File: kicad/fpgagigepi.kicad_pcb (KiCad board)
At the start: 4 copper layers, 65 x 56 mm, 142 parts, among them J1 BH-10(IDC-10MS), J2 PLS-2, J3 PBD-40(DS1023-2x20), J4 PLD-10(DS1021-2x5), J5 L829-1J1T-43, J6 POE connector, J7 PLS-1, J8 PLS-1, J9 PLS-1, U1 CAT24C32WI, U10 TLV62084DSGR, U11 TLV62084DSGR, U2 ASEMB-25.000MHZ-LC-T, U3 NUP4114UPXV6T1G, U4 NB3L553MNR, U5 10CL025ZE144, U6 KSZ9021GN, U7 NUP4114UPXV6T1G, U8 NUP4114UPXV6T1G, U9 TLV62084DSGR

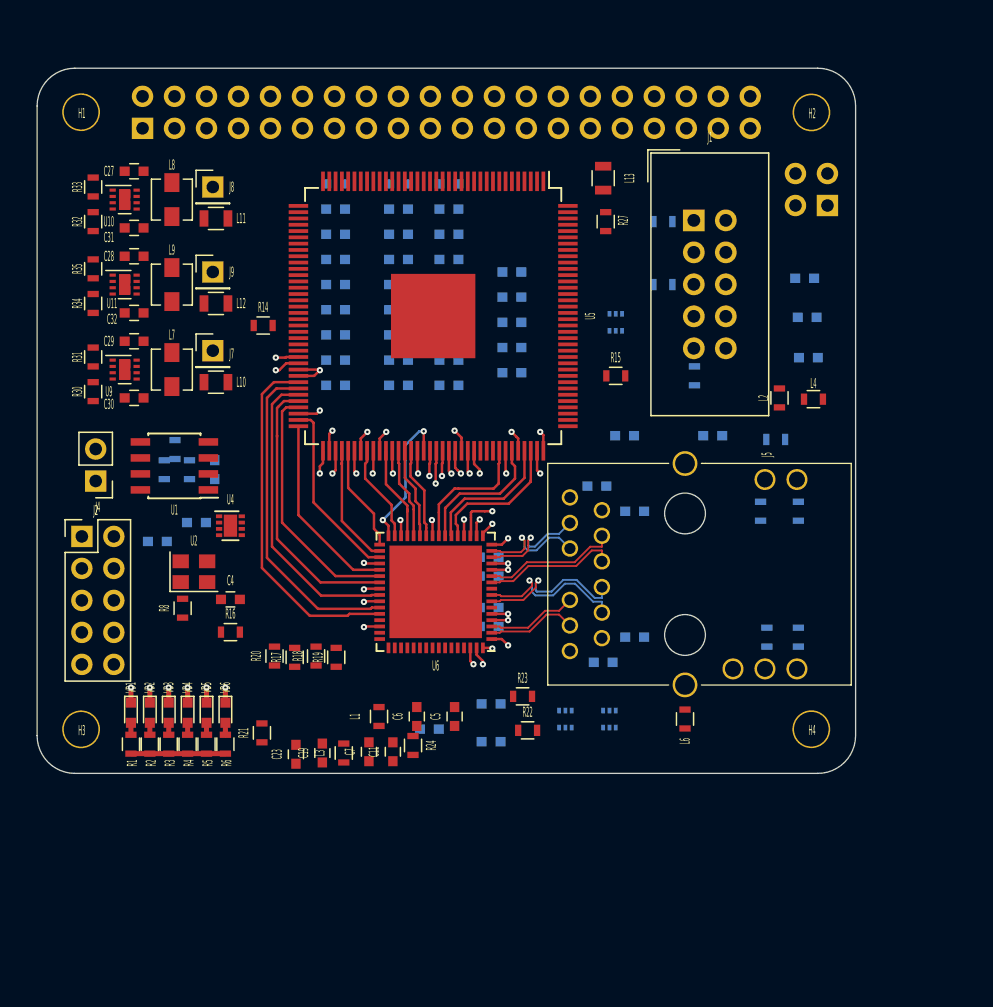
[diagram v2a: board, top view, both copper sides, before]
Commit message: Replaced clock buffer NB3L553DR2G to cdclvc1102 Added datasheet for cdclvc1102 Added components cdclvc1102pw in library_cache Remaped cyclone-to-40-pin-header connections Updated schematics Updated PCB - all signal routed. Power connections not routed Updated BOM file (non-altium format)
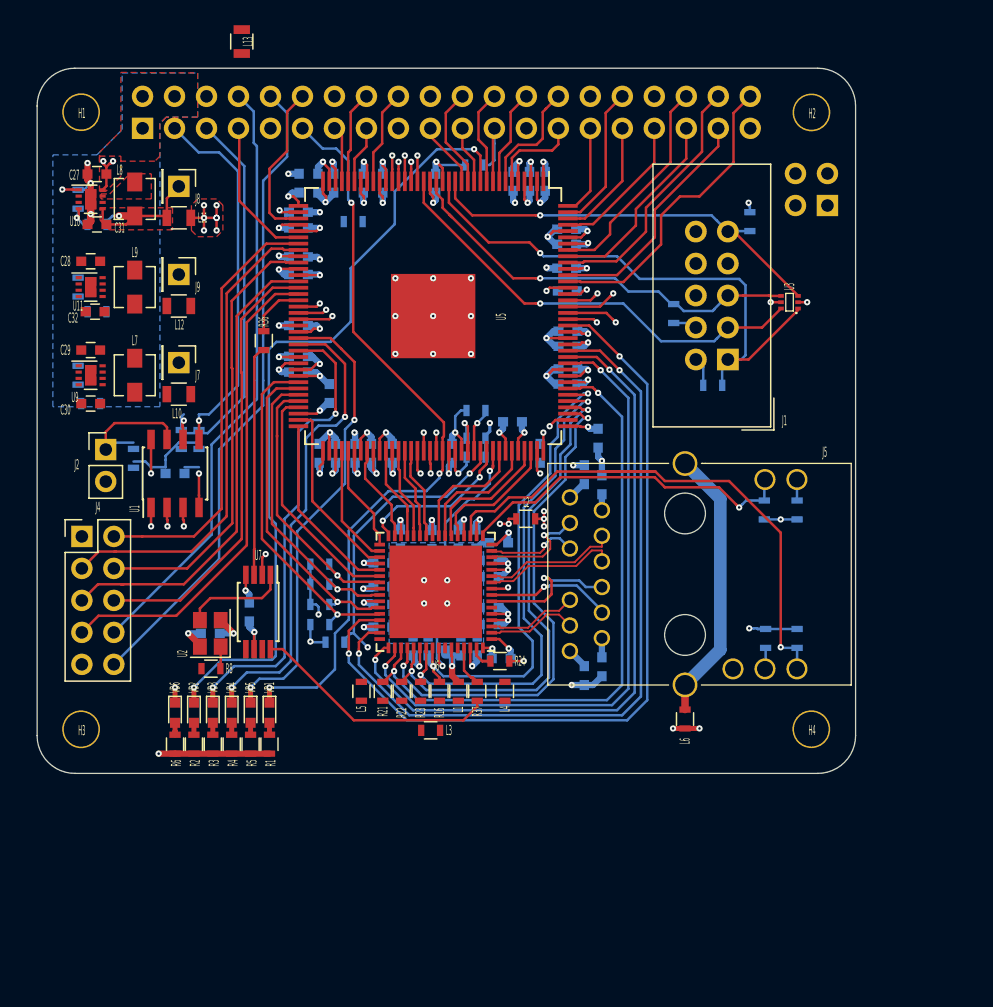
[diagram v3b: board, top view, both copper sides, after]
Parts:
- removed U4: NB3L553MNR, Housings_DFN_QFN:DFN-8-1EP_2x2mm_Pitch0.5mm
- removed U8: NUP4114UPXV6T1G, library:SOT-563-6
- added C65: 0.1u, Capacitors_SMD:C_0603, B.Cu at (103.8, 91.4)
- added C66: 0.1u, Capacitors_SMD:C_0603, B.Cu at (101.8, 86.7)
- added R36: 33R, Resistors_SMD:R_0603, F.Cu at (96.5, 82.5)
- added R37: 33R, Resistors_SMD:R_0603, F.Cu at (113.5, 110.3)
- added R38: 33R, Resistors_SMD:R_0603, B.Cu at (113.4, 91.7)
- added R39: 33R, Resistors_SMD:R_0603, B.Cu at (113.4, 90.2)
- added R40: 33R, Resistors_SMD:R_0603, B.Cu at (113.4, 88.0)
- C11, C19, C23, C4, C5, C6, C7, R14, R15, R17, R18, R19, R20, R27, R30, R31, R32, R33, R34, R35: moved to B.Cu
- L5, U3: moved to F.Cu
- U7: value NUP4114UPXV6T1G -> CDCLVC1102PW; footprint library:SOT-563-6 -> Housings_SSOP:TSSOP-8_4.4x3mm_Pitch0.65mm; moved to F.Cu
- moved R27 39.7 mm to (102.2, 106.4), turned to 0 degrees
- moved L5 38.5 mm to (104.3, 110.3), turned to 270 degrees
- moved C22 37.0 mm to (113.5, 106.7), turned to 90 degrees
- moved C18 34.2 mm to (115.4, 107.7), turned to 180 degrees
- moved L4 33.7 mm to (115.7, 110.3), turned to 270 degrees
- moved C10 32.1 mm to (115.2, 98.5), turned to 180 degrees
- moved L13 30.7 mm to (94.8, 58.7), turned to 90 degrees
- moved U7 25.8 mm to (96.1, 104.0), turned to 270 degrees
- moved L2 22.3 mm to (117.3, 96.6), turned to 0 degrees
- moved C23 22.3 mm to (113.4, 98.2), turned to 270 degrees
- moved C63 21.9 mm to (106.8, 91.4), turned to 90 degrees
- moved C9 21.8 mm to (112.0, 98.2), turned to 270 degrees
- moved C57 20.7 mm to (102.1, 70.0), turned to 270 degrees
- moved R15 20.1 mm to (113.3, 68.5), turned to 180 degrees
- moved C37 20.0 mm to (123.1, 90.2), turned to 270 degrees
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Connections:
- net AVDDL renamed /ethernet.sch/AVDDL
- net DVDDL renamed /ethernet.sch/DVDDL
- net Net-(C10-Pad1) renamed /ethernet.sch/AVDDH
- net Net-(C30-Pad1) renamed /power.sch/2.5V_out
- net Net-(C31-Pad1) renamed /power.sch/3.3V_out
- net Net-(C32-Pad1) renamed /power.sch/1.2V_out
- net Net-(C5-Pad1) renamed /ethernet.sch/AVDDL_PLL
- C3 pad 1: +3V3 -> GND
- C3 pad 2: GND -> +3V3
- J3 pad 12: IO_51 -> IO_39
- J3 pad 13: nSTATUS -> IO_99
- J3 pad 15: nCONFIG -> IO_85
- J3 pad 16: IO_6 -> IO_86
- J3 pad 18: IO_8 -> IO_87
- J3 pad 19: DATA -> nCONFIG
- J3 pad 21: IO_99 -> DCLK
- J3 pad 22: IO_85 -> DATA
- J3 pad 23: DCLK -> nSTATUS
- J3 pad 24: IO_86 -> IO_10
- J3 pad 25: Net-(J3-Pad25) -> GND
- J3 pad 26: IO_87 -> IO_8
- J3 pad 27: Net-(J3-Pad27) -> IO_6
- J3 pad 28: Net-(J3-Pad28) -> IO_7
- J3 pad 29: IO_76 -> IO_144
- J3 pad 31: IO_77 -> IO_142
- J3 pad 32: IO_98 -> IO_143
- J3 pad 33: IO_80 -> IO_141
- J3 pad 37: IO_83 -> IO_133
- J3 pad 39: Net-(J3-Pad25) -> GND
- J3 pad 7: IO_50 -> IO_42
- J3 pad 9: Net-(J3-Pad25) -> GND
- J4 pad 1: +5V -> +3V3
- J4 pad 2: /interface.sch/IO_44 -> /interface.sch/IO_43
- J4 pad 3: /interface.sch/IO_39 -> /interface.sch/IO_44
- J4 pad 5: /interface.sch/IO_42 -> /interface.sch/IO_49
- J4 pad 6: /interface.sch/IO_49 -> /interface.sch/IO_50
- J4 pad 7: /interface.sch/IO_43 -> /interface.sch/IO_51
- R27 pad 2: /ethernet.sch/RX_CLK -> RX_CLK
- U3 pad 1: JTAG_TDO -> JTAG_TCK
- U3 pad 3: JTAG_TMS -> JTAG_TDI
- U3 pad 4: JTAG_TDI -> JTAG_TMS
- U3 pad 6: JTAG_TCK -> JTAG_TDO
- U5 pad 10: USER_LED0 -> IO_10
- U5 pad 100: Net-(U5-Pad100) -> TX_CLK
- U5 pad 11: USER_LED1 -> USER_LED0
- U5 pad 111: Net-(U5-Pad111) -> /ethernet.sch/COL
- U5 pad 112: IO_76 -> INT_N
- U5 pad 113: IO_77 -> CLK_125M
- U5 pad 114: IO_80 -> /ethernet.sch/RESET_N
- U5 pad 115: IO_83 -> /ethernet.sch/MDIO
- U5 pad 119: IO_85 -> /ethernet.sch/MDC
- U5 pad 120: IO_86 -> /ethernet.sch/CRS
- U5 pad 121: IO_87 -> /ethernet.sch/RX_ER
- U5 pad 125: Net-(U5-Pad125) -> /ethernet.sch/RX_DV
- U5 pad 132: Net-(U5-Pad132) -> PI_GPIO21/SPI1_SCLK
- U5 pad 133: Net-(U5-Pad133) -> IO_133
- U5 pad 135: /ethernet.sch/RX_DV -> PI_GPIO20/SPI1_MOSI
- U5 pad 136: /ethernet.sch/RX_ER -> PI_GPIO19/SPI1_MISO
- U5 pad 137: /ethernet.sch/COL -> PI_GPIO16/SPI1_CS0
- U5 pad 141: /ethernet.sch/CRS -> IO_141
- U5 pad 142: /ethernet.sch/MDC -> IO_142
- U5 pad 143: /ethernet.sch/MDIO -> IO_143
- U5 pad 144: /ethernet.sch/RESET_N -> IO_144
- U5 pad 28: PI_GPIO19/SPI1_MISO -> IO_87
- U5 pad 31: PI_GPIO20/SPI1_MOSI -> IO_85
- U5 pad 32: PI_GPIO21/SPI1_SCLK -> IO_86
- U5 pad 33: PI_GPIO16/SPI1_CS0 -> IO_99
- U5 pad 39: /interface.sch/IO_39 -> IO_39
- U5 pad 42: /interface.sch/IO_42 -> IO_42
- U5 pad 50: IO_50 -> /interface.sch/IO_50
- U5 pad 51: IO_51 -> /interface.sch/IO_51
- U5 pad 52: GND -> 25M_A
- U5 pad 54: Net-(U5-Pad54) -> GND
- U5 pad 55: /ethernet.sch/RX_CLK -> GND
- U5 pad 58: Net-(U5-Pad58) -> USER_LED3
- U5 pad 59: Net-(U5-Pad59) -> USER_LED2
- U5 pad 60: Net-(U5-Pad60) -> USER_LED1
- U5 pad 7: INT_N -> IO_7
- U5 pad 88: /ethernet.sch/TX_CLK -> GND
- U5 pad 89: /ethernet.sch/GTX_CLK -> GND
- U5 pad 94: GND -> Net-(R38-Pad1)
- U5 pad 96: GND -> Net-(R39-Pad1)
- U5 pad 97: GND -> Net-(R40-Pad1)
- U5 pad 98: Net-(U5-Pad98) -> RX_CLK
- U5 pad 99: Net-(U5-Pad99) -> GTX_CLK
- U6 pad 32: /ethernet.sch/GTX_CLK -> GTX_CLK
- U6 pad 48: /ethernet.sch/RX_CLK -> RX_CLK
- U6 pad 57: /ethernet.sch/TX_CLK -> TX_CLK
- U7 pad 1: /ethernet.sch/TXRXA+ -> Net-(U2-Pad3)
- U7 pad 2: GND -> +3V3
- U7 pad 3: /ethernet.sch/TXRXA- -> Net-(R36-Pad2)
- U7 pad 4: /ethernet.sch/TXRXB+ -> GND
- U7 pad 6: /ethernet.sch/TXRXB- -> +3V3
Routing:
- net GND: track 29.7 -> 221.8 mm, vias 14 -> 78
- net /ethernet.sch/RX_DV: track 0.00 -> 64.9 mm, vias 0 -> 2
- net USER_LED0: track 1.20 -> 63.0 mm, vias 1 -> 2
- net /ethernet.sch/RX_ER: track 0.00 -> 59.8 mm, vias 0 -> 2
- net +3V3: track 13.2 -> 70.8 mm, vias 3 -> 29
- net CONF_DONE: track 3.22 -> 60.6 mm, vias 2 -> 3
- net /ethernet.sch/CRS: track 0.00 -> 55.2 mm, vias 0 -> 2
- net /ethernet.sch/MDC: track 0.00 -> 52.4 mm, vias 0 -> 2
- net UART0_RX: track 0.00 -> 51.4 mm
- net /ethernet.sch/MDIO: track 0.00 -> 49.7 mm, vias 0 -> 2
- net UART0_TX: track 0.00 -> 47.9 mm
- net JTAG_TCK: track 0.00 -> 44.6 mm, vias 0 -> 1
- net MDI_LED_G: track 3.71 -> 45.8 mm
- net INT_N: track 0.00 -> 41.0 mm, vias 0 -> 2
- net /ethernet.sch/COL: track 0.00 -> 40.6 mm, vias 0 -> 2
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- added copper zone on F.Cu, net +3V3
- added copper zone on B.Cu, net +5V
- added copper zone on F.Cu, net +5V
- added copper zone on F.Cu, net /power.sch/3.3V_out
- added copper zone on B.Cu, net GND
- added copper zone on In1.Cu, net GND
- added copper zone on F.Cu, net Net-(L8-Pad1)
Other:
- net class Default: clearance 0.15 -> 0.125
- rule trace_clearance: 0.15 -> 0.125
